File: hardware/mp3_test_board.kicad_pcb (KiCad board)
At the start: 4 copper layers, 100 x 56 mm, 224 parts, among them J1 TF01-A, J2 PJ-322, P1 WF24LTYAJDNN0#, P2 USB-TYPE-C-018, Q1 2N7002K, SW1 K2-1156SP-F5SW-05, SW2 K2-1156SP-F5SW-05, SW3 K2-1156SP-F5SW-05, SW4 K2-1156SP-F5SW-05, SW5 K2-1156SP-F5SW-05, SW6 GT-TC054A-H035-L1, SW7 GT-TC054A-H035-L1, SW8 GT-TC054A-H035-L1, U1 F133, U10 SGM6603-ADJYN6G, U11 SGM3204, U2 USBLC6-2SC6, U3 MX25L25645GM2I-08G, U4 PCM1795, U5 LM4562, U6 LM4562, U7 OPA1656, U8 OPA1656, U9 AXP2101, Y1 12.88727, Y2 26МHz

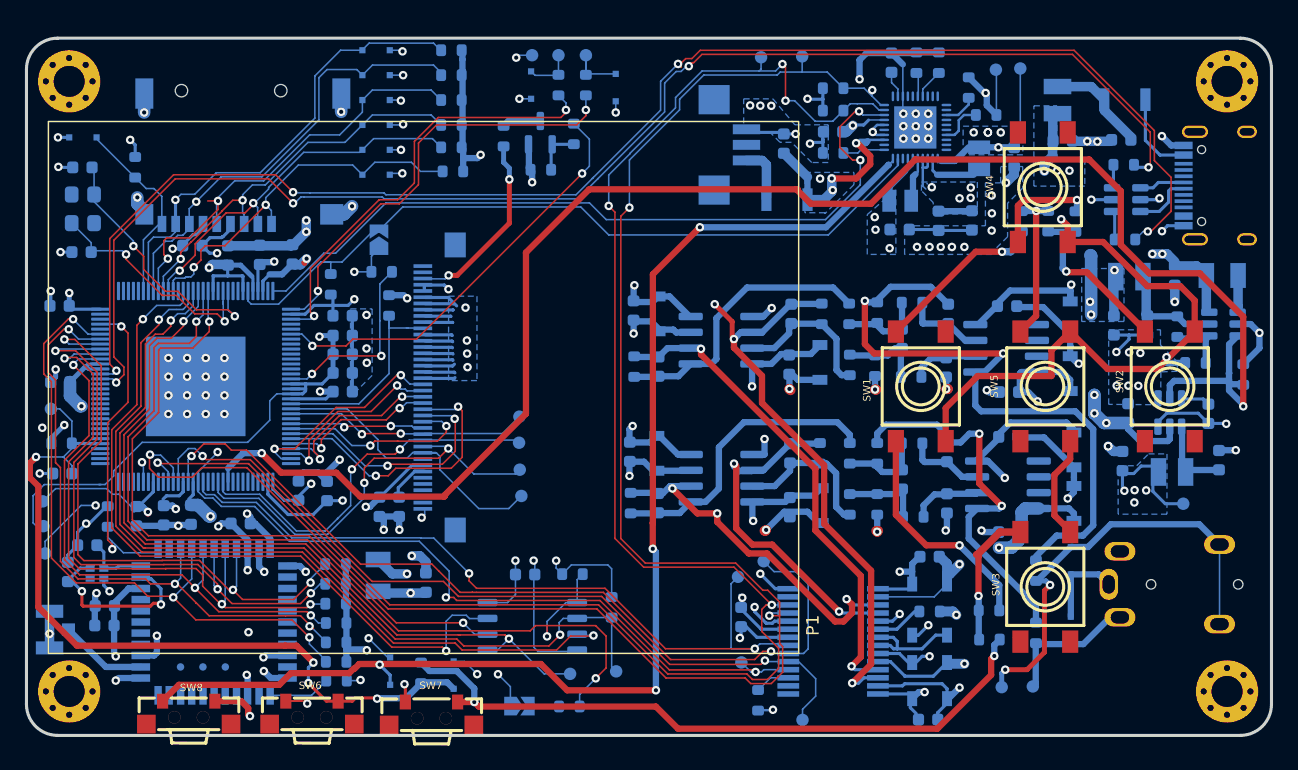
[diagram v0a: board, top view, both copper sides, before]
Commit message: some changes on fab layers
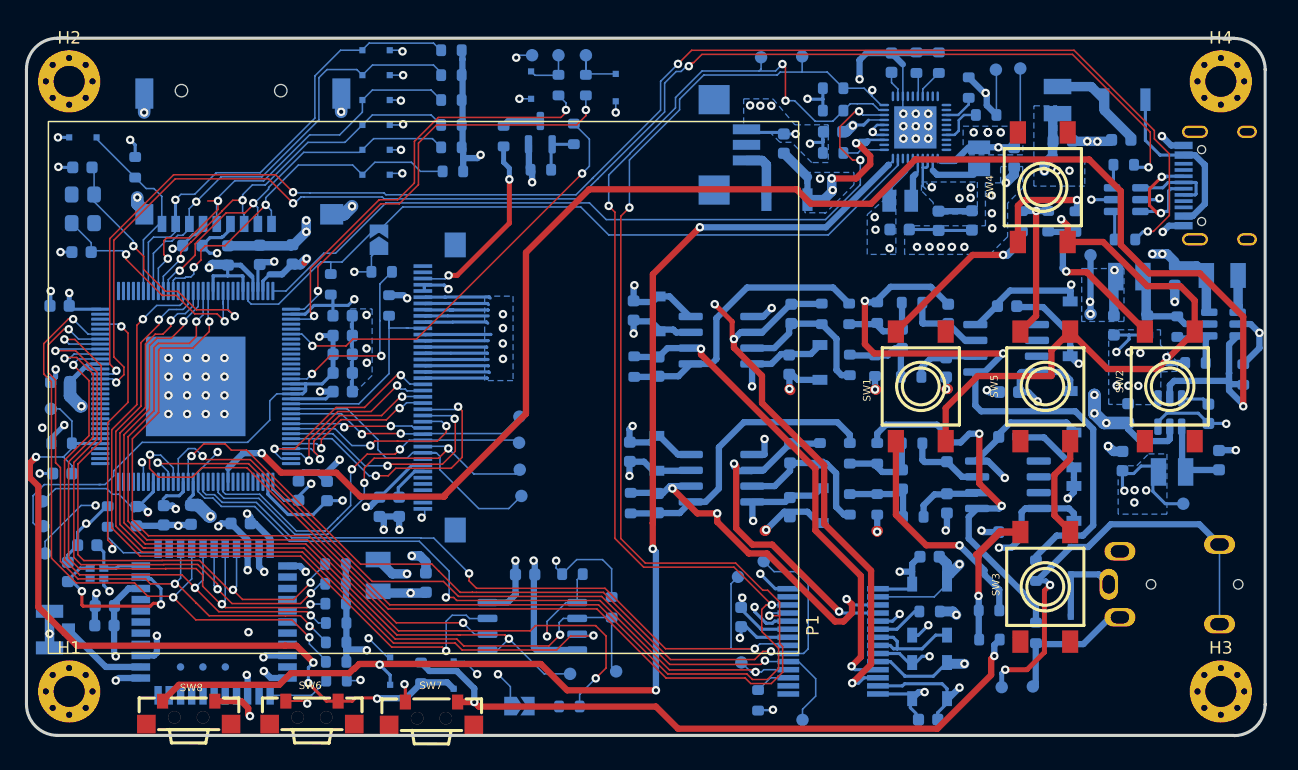
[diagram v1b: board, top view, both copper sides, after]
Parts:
- H1, H2, H3, H4: footprint MountingHole:MountingHole_2.5mm_Pad_Via -> rlib_misc:MountingHole_2.5mm_Pad_Via
- TP1, TP10, TP11, TP12, TP13, TP14, TP15, TP16, TP17, TP18, TP19, TP2, TP20, TP21, TP22, TP23, TP24, TP25, TP3, TP4, TP5, TP6, TP7, TP8, TP9: footprint TestPoint:TestPoint_Pad_D1.0mm -> rlib_misc:TestPoint_Pad_D1.0mm
- moved H3 0.50 mm to (172.4, 95.7)
- moved H4 0.50 mm to (172.4, 46.7)
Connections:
- P2 pad B6: (no net) -> Net-(P2-PadA6)
- P2 pad B7: (no net) -> Net-(P2-PadA7)
- U1 pad 55: /SOC/LCD_D2 -> unconnected-(U1-Pad55)
- U1 pad 64: /SOC/LCD_D13 -> unconnected-(U1-Pad64)
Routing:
- net GND: track 347.4 -> 392.0 mm
- net unconnected-(SW3-Pad4): track 8.35 -> 0.00 mm
- net Net-(F1-Pad2): track 6.83 -> 14.1 mm
- net Net-(P2-PadA7): track 4.75 -> 11.0 mm, vias 0 -> 2
- net Net-(P2-PadA6): track 3.65 -> 6.59 mm
- net VCC: track 61.3 -> 64.1 mm
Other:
- board size 100 x 56 mm -> 99.5 x 56 mm

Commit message: pwr btn is optional connected to soc
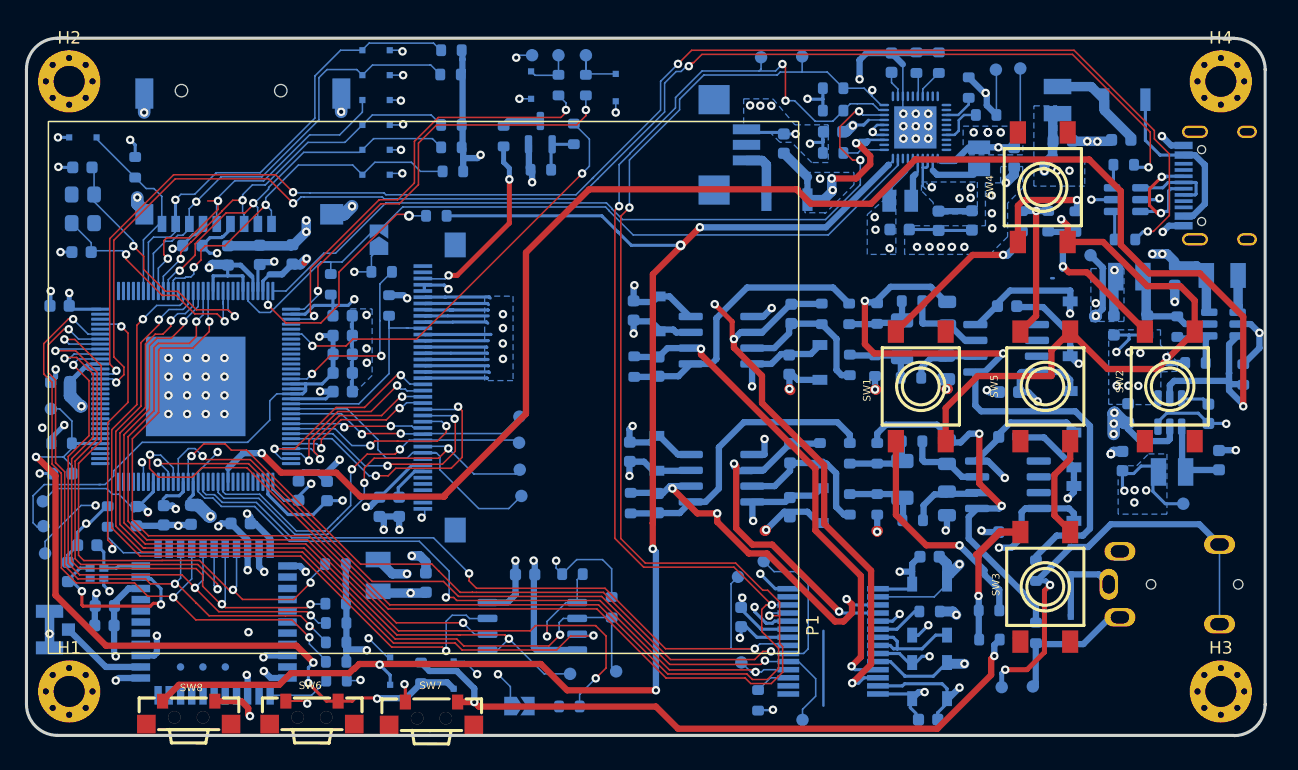
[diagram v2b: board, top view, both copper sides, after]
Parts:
- removed R61: 10k, rlib_passive:R_0603_1608Metric
- C47, C48: footprint rlib_passive:C_0603_1608Metric -> rlib_passive:C_1206_3216Metric
- C49, C50, C51, C52: footprint rlib_passive:C_0603_1608Metric -> rlib_passive:C_0805_2012Metric
- R18: value 10k -> 0
- moved R18 9.38 mm to (109.4, 57.5)
- moved R40 0.28 mm to (147.7, 82.0)
- moved R39 0.17 mm to (147.6, 75.6)
- moved R37 0.12 mm to (147.6, 64.3)
- moved R56 0.09 mm to (110.5, 46.1)
- moved C49 0.08 mm to (150.4, 65.4)
- moved R33 0.08 mm to (144.8, 65.3)
- moved R38 0.07 mm to (147.5, 70.5)
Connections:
- R18 pad 1: +3V3 -> Net-(D12-Pad1)
- R18 pad 2: /SOC/SDC_CLK -> /Power/PWR_KEY
- U1 pad 31: unconnected-(U1-Pad31) -> /Power/PWR_KEY
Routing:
- net Net-(D12-Pad1): track 100.5 -> 120.2 mm, vias 4 -> 5
- net /Power/PWR_KEY: track 0.00 -> 19.7 mm, vias 0 -> 2
- net /SOC/WIFI_SDIO_CLK: track 49.4 -> 39.5 mm, vias 3 -> 2
- net GND: track 392.0 -> 383.3 mm
- net unconnected-(SW3-Pad4): track 0.00 -> 8.35 mm
- net /SOC/SDC_CLK: track 35.5 -> 28.9 mm
- net +5VA: track 166.7 -> 170.3 mm
- net -5VA: track 150.6 -> 152.9 mm
- net /SOC/KEYS: track 62.9 -> 61.1 mm
- net Net-(C48-Pad2): track 6.85 -> 5.68 mm
- net Net-(C47-Pad2): track 6.78 -> 5.81 mm
- net Net-(C47-Pad1): track 6.79 -> 5.91 mm
- net Net-(C48-Pad1): track 6.62 -> 5.88 mm
- net /Power/RESET: track 61.5 -> 62.1 mm

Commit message: ferrite bead in adc power net is added
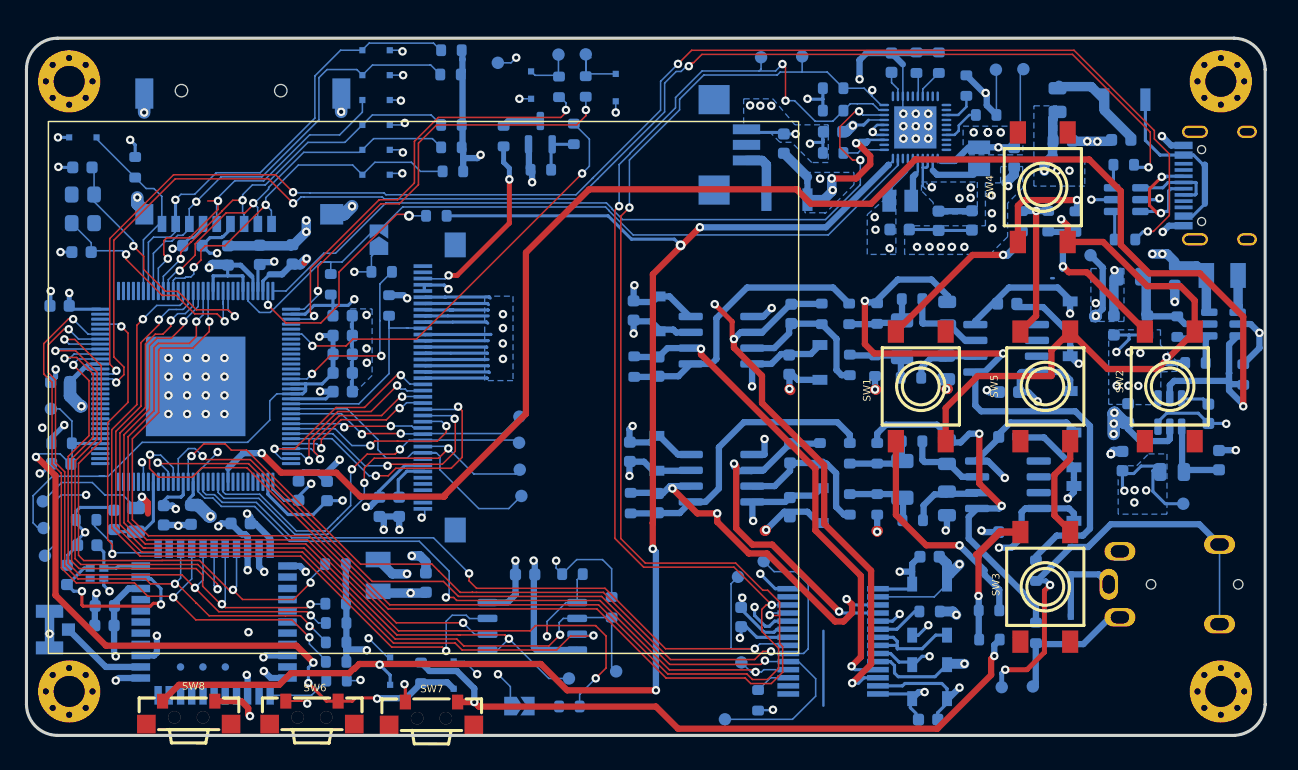
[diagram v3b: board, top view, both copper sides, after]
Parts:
- added FB1: FerriteBead, rlib_passive:C_0805_2012Metric, B.Cu at (85.3, 81.9)
- FB1, FB2, FB3: footprint rlib_passive:INDC2520X120N -> rlib_passive:C_0805_2012Metric
- moved TP21 6.23 mm to (132.6, 97.9)
- moved TP8 2.82 mm to (114.3, 45.2)
- moved C22 1.83 mm to (83.5, 81.9), turned to 90 degrees
- moved R64 1.75 mm to (81.3, 81.9), turned to 180 degrees
- moved C3 0.79 mm to (79.3, 77.4)
- moved TP12 0.38 mm to (120.0, 94.7)
- moved TP16 0.25 mm to (156.5, 45.7)
- moved R50 0.25 mm to (152.0, 47.0)
- moved C76 0.25 mm to (79.7, 86.3)
- moved C45 0.19 mm to (155.2, 64.6)
- moved TP17 0.19 mm to (78.0, 84.8)
- moved C37 0.17 mm to (147.4, 92.8)
- moved R37 0.16 mm to (147.6, 64.2)
- moved TP7 0.16 mm to (77.8, 82.6)
- moved R52 0.15 mm to (119.2, 47.1)
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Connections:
- C22 pad 1: +1V8A -> Net-(C22-Pad1)
- U1 pad 89: +1V8A -> Net-(C22-Pad1)
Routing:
- net GND: track 383.3 -> 394.7 mm
- net unconnected-(SW3-Pad4): track 8.35 -> 0.00 mm
- net Net-(C22-Pad1): track 0.00 -> 7.33 mm
- net /NewDAC/I2S_DIN: track 64.3 -> 70.0 mm
- net /SOC/WIFI_REG_ON: track 27.0 -> 28.9 mm
- net +0V9: track 136.1 -> 137.3 mm
- net +1V8A: track 62.7 -> 61.8 mm
- net Net-(C49-Pad2): track 52.2 -> 53.1 mm
- net +3V3: track 404.7 -> 405.4 mm

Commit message: some fixes
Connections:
- U1 pad 114: /SOC/USB_DP -> /SOC/USB_DM
- U1 pad 115: /SOC/USB_DM -> /SOC/USB_DP
- U1 pad 122: /SOC/WIFI_SDIO_D2 -> /SOC/WIFI_SDIO_D3
- U1 pad 123: /SOC/WIFI_SDIO_D3 -> /SOC/WIFI_SDIO_D2
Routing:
- net GND: track 394.7 -> 386.3 mm
- net unconnected-(SW3-Pad4): track 0.00 -> 8.35 mm
- net /SOC/USB_DP: track 112.7 -> 111.5 mm
- net /SOC/USB_DM: track 118.9 -> 120.0 mm

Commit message: xxx
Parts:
- removed TP7: TestPoint, rlib_misc:TestPoint_Pad_D1.0mm
- C31: value 10u -> 47u
- R6: value 100 -> 50
- moved C77 0.14 mm to (81.2, 84.0)
- moved C64 0.12 mm to (155.8, 52.9)
- moved R64 0.06 mm to (81.2, 82.0)
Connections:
- R5 pad 1: +3V3 -> +1V8A
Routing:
- net +1V8B: track 52.5 -> 23.7 mm
- net unconnected-(SW3-Pad4): track 8.35 -> 0.00 mm
- net +1V8A: track 61.8 -> 66.5 mm
- net GND: track 386.3 -> 390.4 mm
- net /SOC/KEYS: track 60.9 -> 57.3 mm
- net +3V3: track 405.4 -> 403.5 mm, vias 26 -> 25
- net +5VA: track 170.1 -> 168.2 mm, vias 14 -> 12
- net VCC: track 64.4 -> 65.9 mm, vias 8 -> 9
- net Net-(C71-Pad2): track 7.02 -> 5.58 mm, vias 1 -> 0
- net +0V9: track 137.3 -> 136.1 mm
- net -5VA: track 152.7 -> 153.8 mm
- net /SOC/WIFI_REG_ON: track 28.9 -> 27.9 mm
- net /Power/RESET: track 62.1 -> 62.6 mm
